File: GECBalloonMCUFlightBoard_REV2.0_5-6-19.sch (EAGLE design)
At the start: 57 parts, among them IC1 PIC32MX360F512L, Q1 IRF3704L-V, Q2 IRF3704L-V, U1 ADS1118, U2 ADS1118, X2 MALE_VGA, Y1 SG-636PCW_50.0000MC3__ROHS

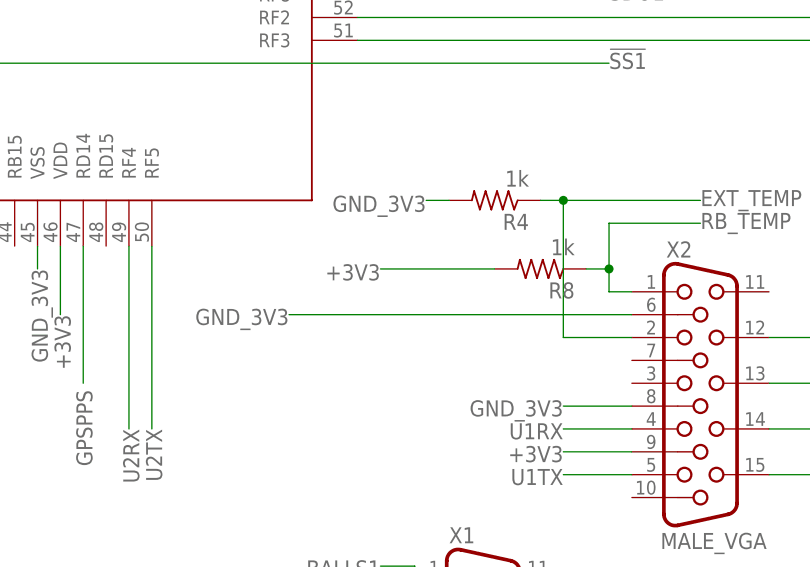
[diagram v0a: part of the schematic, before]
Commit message: Added another ground pin to the DB15 connector and fixed the resistor layout to work with the temp sensors
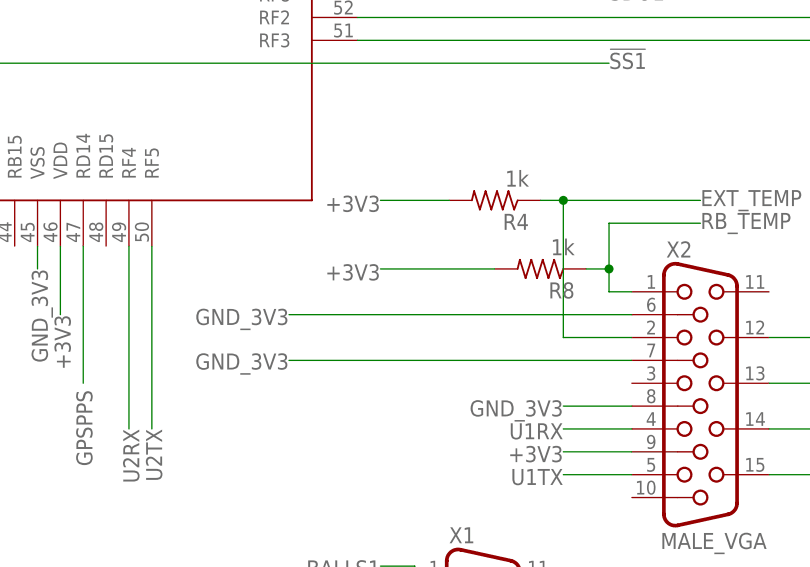
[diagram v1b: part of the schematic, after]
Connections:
- net +3V3: now also R4.2
- net GND_3V3: now also X2.7; no longer R4.2
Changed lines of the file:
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@@
 <pinref part="Q2" gate="G$1" pin="S"/>
+</segment>
+<segment>
+<pinref part="R4" gate="G$1" pin="2"/>
+<wire x1="134.62" y1="12.7" x2="127" y2="12.7" width="0.1524" layer="91"/>
+<label x="127" y="13.208" size="1.778" layer="95" rot="R180"/>
 </segment>
 </net>
@@
 </segment>
 <segment>
-<pinref part="R4" gate="G$1" pin="2"/>
-<wire x1="134.62" y1="12.7" x2="132.08" y2="12.7" width="0.1524" layer="91"/>
-<label x="132.08" y="13.208" size="1.778" layer="95" rot="R180"/>
-</segment>
-<segment>
 <wire x1="154.94" y1="-10.16" x2="147.32" y2="-10.16" width="0.1524" layer="91"/>
 <label x="147.32" y="-9.525" size="1.778" layer="95" rot="R180"/>
@@
 <wire x1="175.26" y1="116.84" x2="187.96" y2="116.84" width="0.1524" layer="91"/>
 </segment>
+<segment>
+<pinref part="X2" gate="G$1" pin="7"/>
+<wire x1="154.94" y1="-5.08" x2="116.84" y2="-5.08" width="0.1524" layer="91"/>
+<label x="116.84" y="-4.318" size="1.778" layer="95" rot="R180"/>
+</segment>
 </net>

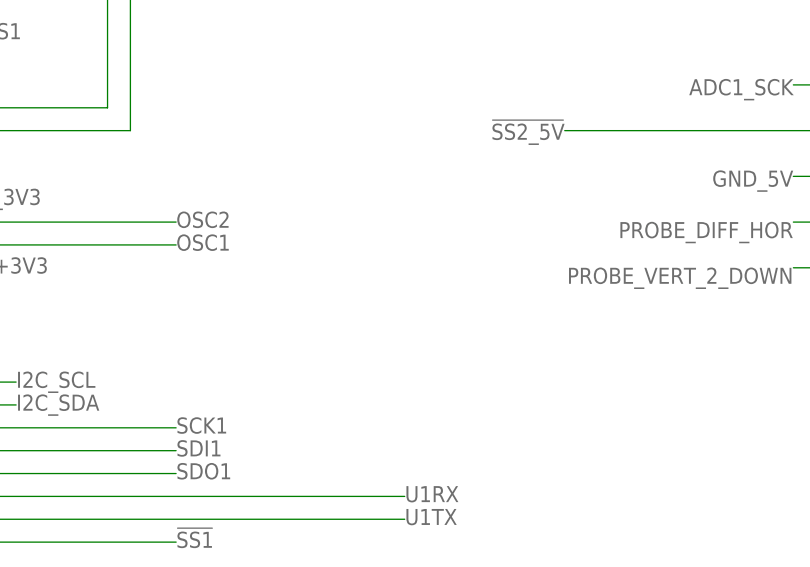
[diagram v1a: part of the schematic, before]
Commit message: Added onboard I2C pullup resistors
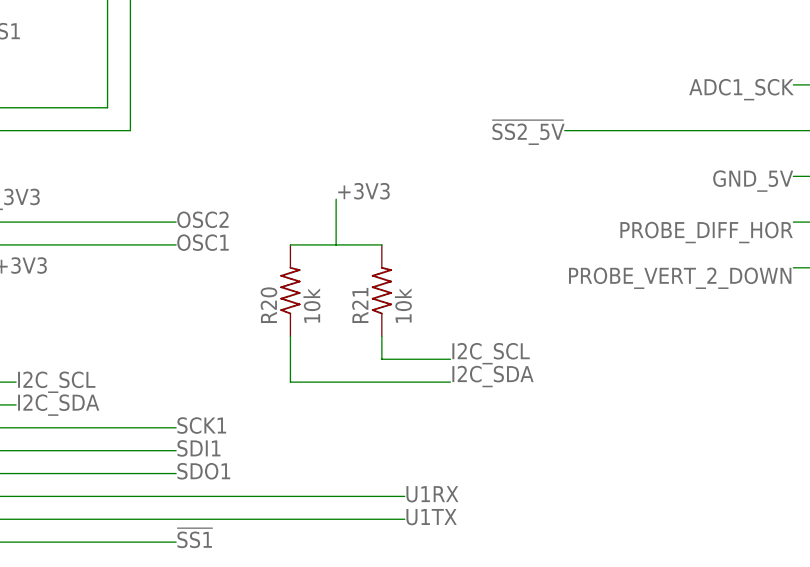
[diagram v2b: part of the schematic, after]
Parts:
- added R20, R21: 10k, rcl:R-US_M1206
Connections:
- net +3V3: now also R20.2, R21.2
- net I2C_SCL: now also R21.1
- net I2C_SDA: now also R20.1
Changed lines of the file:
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@@
 <part name="R18" library="resistor" deviceset="R-US_" device="R1206" value="680"/>
 <part name="R19" library="resistor" deviceset="R-US_" device="R1206" value="510"/>
+<part name="R20" library="rcl" deviceset="R-US_" device="M1206" value="10k"/>
+<part name="R21" library="rcl" deviceset="R-US_" device="M1206" value="10k"/>
 </parts>
 <sheets>
@@
 <instance part="R18" gate="G$1" x="406.4" y="109.22" rot="MR0"/>
 <instance part="R19" gate="G$1" x="396.24" y="101.6"/>
+<instance part="R20" gate="G$1" x="165.1" y="55.88" rot="R90"/>
+<instance part="R21" gate="G$1" x="175.26" y="55.88" rot="R90"/>
 </instances>
 <busses>
@@
 <wire x1="134.62" y1="12.7" x2="127" y2="12.7" width="0.1524" layer="91"/>
 <label x="127" y="13.208" size="1.778" layer="95" rot="R180"/>
+</segment>
+<segment>
+<pinref part="R20" gate="G$1" pin="2"/>
+<pinref part="R21" gate="G$1" pin="2"/>
+<wire x1="165.1" y1="60.96" x2="170.18" y2="60.96" width="0.1524" layer="91"/>
+<wire x1="175.26" y1="60.96" x2="170.18" y2="60.96" width="0.1524" layer="91"/>
+<wire x1="170.18" y1="60.96" x2="170.18" y2="66.04" width="0.1524" layer="91"/>
+<label x="170.18" y="66.04" size="1.778" layer="95"/>
 </segment>
 </net>
@@
 <label x="134.62" y="45.085" size="1.778" layer="95"/>
 </segment>
+<segment>
+<pinref part="R21" gate="G$1" pin="1"/>
+<wire x1="175.26" y1="50.8" x2="175.26" y2="48.26" width="0.1524" layer="91"/>
+<wire x1="175.26" y1="48.26" x2="182.88" y2="48.26" width="0.1524" layer="91"/>
+<label x="182.88" y="48.26" size="1.778" layer="95"/>
+</segment>
 </net>
 <net name="I2C_SDA" class="0">
@@
 <label x="134.62" y="42.545" size="1.778" layer="95"/>
 </segment>
-</net>
+<segment>
+<pinref part="R20" gate="G$1" pin="1"/>
+<wire x1="165.1" y1="50.8" x2="165.1" y2="45.72" width="0.1524" layer="91"/>
+<wire x1="165.1" y1="45.72" x2="182.88" y2="45.72" width="0.1524" layer="91"/>
+<label x="182.88" y="45.72" size="1.778" layer="95"/>
+</segment>
+</net>
